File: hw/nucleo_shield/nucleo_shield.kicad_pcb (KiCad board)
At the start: 2 copper layers, 100 x 70 mm, 36 parts, among them CN101 Nucleo-F411RE-CN10, CN71 Nucleo-F411RE-CN7, P1 CONN_01X10, P2 CONN_01X10, P3 CONN_01X10, P4 CONN_01X02, P5 CONN_01X06, U1 74HC595, U2 74HC595, U3 LTV-847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

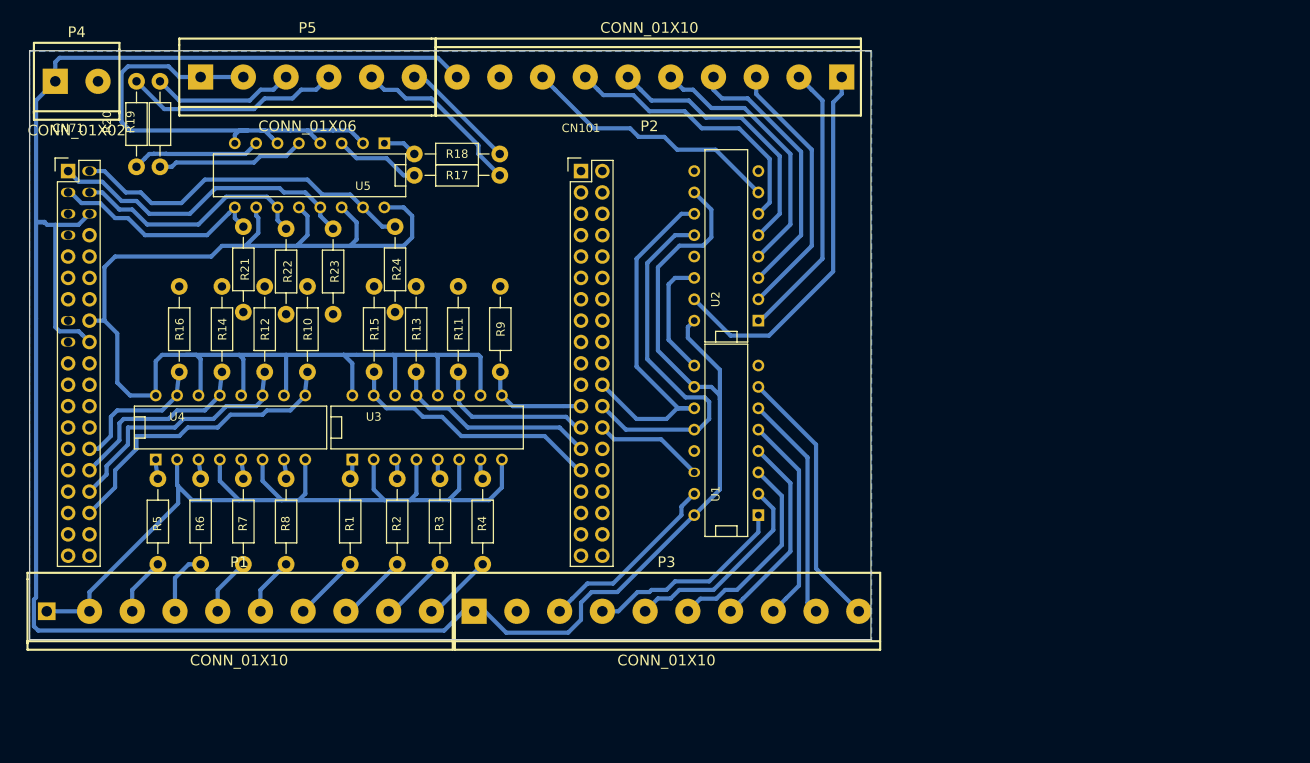
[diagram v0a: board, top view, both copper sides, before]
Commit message: HW: modify nucleo with hierarchical sheets
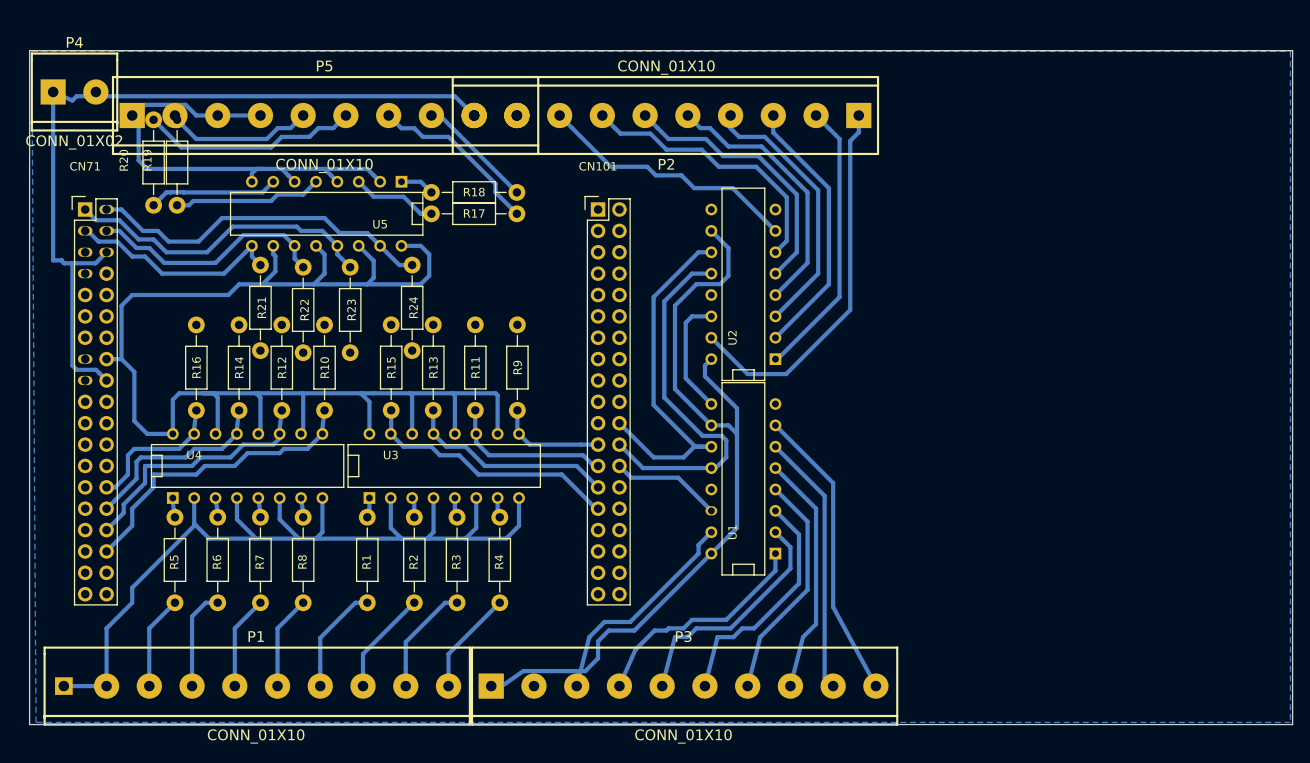
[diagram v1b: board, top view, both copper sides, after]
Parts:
- P5: value CONN_01X06 -> CONN_01X10; footprint w_conn_screw:mors_6p -> w_conn_screw:mors_10p
- moved P3 9.12 mm to (173.2, 144.0)
- moved P1 9.12 mm to (122.4, 144.0)
- moved R3 5.00 mm to (146.3, 129.0)
- moved R7 5.00 mm to (122.9, 129.0)
- moved R5 5.00 mm to (112.8, 129.0)
- moved R6 5.00 mm to (117.9, 129.0)
- moved R8 5.00 mm to (128.0, 129.0)
- moved R1 5.00 mm to (135.6, 129.0)
- moved R2 5.00 mm to (141.2, 129.0)
- moved R4 5.00 mm to (151.4, 129.0)
- moved CN101 5.00 mm to (163.1, 87.4)
- moved CN71 5.00 mm to (102.1, 87.4)
- moved P2 5.00 mm to (171.2, 76.2)
- moved P5 5.00 mm to (130.6, 76.2)
- moved R10 5.00 mm to (130.6, 106.2)
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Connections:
- P5 pad 3: inh11 -> inh16
- P5 pad 4: inh12 -> inh15
- P5 pad 5: inh10 -> inh14
- P5 pad 6: inh9 -> inh13
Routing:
- net +5V: track 291.6 -> 192.3 mm
- net inh10: track 20.7 -> 4.61 mm
- net inh16: track 0.00 -> 14.2 mm
- net inh9: track 13.9 -> 0.00 mm
- net inh12: track 25.8 -> 37.6 mm
- net inh14: track 0.00 -> 5.48 mm
- net inh3: track 8.92 -> 14.3 mm
- net inh1: track 9.05 -> 14.2 mm
- net inh2: track 9.19 -> 13.7 mm
- net inh4: track 8.92 -> 13.4 mm
- net inh5: track 7.57 -> 11.9 mm
- net out7: track 27.0 -> 31.3 mm
- net inh8: track 7.79 -> 12.1 mm
- net inh7: track 6.85 -> 11.2 mm
- net inh6: track 8.40 -> 12.7 mm
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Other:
- board size 100 x 70 mm -> 150.1 x 80.1 mm

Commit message: Update schematic to add sct and io expander
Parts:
- added P6: ETH_CONN, Pin_Headers:Pin_Header_Straight_2x04, F.Cu at (235.2, 114.0)
- added P7: SD_CONN, Pin_Headers:Pin_Header_Straight_1x05, F.Cu at (227.1, 114.0)
- added P8: LCD_CONN, Pin_Headers:Pin_Header_Straight_1x09, F.Cu at (218.8, 114.0)
- added R25: R, Resistors_ThroughHole:Resistor_Horizontal_RM10mm, F.Cu at (229.0, 78.8)
- added R26: R, Resistors_ThroughHole:Resistor_Horizontal_RM10mm, F.Cu at (242.5, 78.8)
- added R27: R, Resistors_ThroughHole:Resistor_Horizontal_RM10mm, F.Cu at (229.0, 88.5)
- added R28: R, Resistors_ThroughHole:Resistor_Horizontal_RM10mm, F.Cu at (242.5, 88.5)
- added R29: R, Resistors_ThroughHole:Resistor_Horizontal_RM10mm, F.Cu at (229.0, 98.3)
- added R30: R, Resistors_ThroughHole:Resistor_Horizontal_RM10mm, F.Cu at (256.0, 78.8)
- added R31: R, Resistors_ThroughHole:Resistor_Horizontal_RM10mm, F.Cu at (242.5, 98.3)
- added R32: R, Resistors_ThroughHole:Resistor_Horizontal_RM10mm, F.Cu at (256.0, 88.5)
- added R33: R_LCD_LED, Resistors_ThroughHole:Resistor_Horizontal_RM10mm, F.Cu at (241.6, 112.4)
- added R34: R, Resistors_ThroughHole:Resistor_Horizontal_RM10mm, F.Cu at (224.8, 131.1)
- added U6: LTV-847, Housings_DIP:DIP-16_W7.62mm, F.Cu at (218.2, 80.5)
- added U7: PCF8574A, Housings_DIP:DIP-16_W7.62mm, F.Cu at (276.2, 80.5)
- added U8: PCF8574A, Housings_DIP:DIP-16_W7.62mm, F.Cu at (289.6, 80.5)
- P4: value CONN_01X02 -> POWER_CON
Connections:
- CN101 pad 1: Net-(CN101-Pad1) -> IO_INT
- CN101 pad 11: Net-(CN101-Pad11) -> SPI1_SCK
- CN101 pad 13: Net-(CN101-Pad13) -> SPI1_MISO
- CN101 pad 15: Net-(CN101-Pad15) -> SPI1_MOSI
- CN101 pad 17: Net-(CN101-Pad17) -> SD_CS
- CN101 pad 19: Net-(CN101-Pad19) -> LCD_CS
- CN101 pad 21: Net-(CN101-Pad21) -> LCD_RST
- CN101 pad 23: in4 -> LCD_DC
- CN101 pad 25: in3 -> Net-(CN101-Pad25)
- CN101 pad 27: in2 -> Net-(CN101-Pad27)
- CN101 pad 29: in1 -> Net-(CN101-Pad29)
- CN101 pad 3: Net-(CN101-Pad3) -> I2C1_SCL
- CN101 pad 5: Net-(CN101-Pad5) -> I2C1_SDA
- CN71 pad 1: in10 -> SPI3_SCK
- CN71 pad 2: in9 -> SPI3_MISO
- CN71 pad 28: in5 -> Net-(CN71-Pad28)
- CN71 pad 3: in12 -> SPI3_MOSI
- CN71 pad 30: in6 -> Net-(CN71-Pad30)
- CN71 pad 32: in7 -> Net-(CN71-Pad32)
- CN71 pad 34: in8 -> Net-(CN71-Pad34)
- CN71 pad 4: in11 -> Net-(CN71-Pad4)
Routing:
- net SPI3_MISO: track 0.00 -> 31.2 mm
- net in9: track 41.4 -> 10.2 mm
- net in10: track 37.5 -> 8.23 mm
- net SPI3_SCK: track 0.00 -> 29.2 mm
- net in8: track 36.5 -> 8.30 mm
- net Net-(CN71-Pad34): track 0.00 -> 28.2 mm
- net Net-(CN101-Pad29): track 0.00 -> 22.9 mm
- net in1: track 30.9 -> 8.01 mm
- net in7: track 30.5 -> 15.4 mm
- net Net-(CN71-Pad32): track 0.00 -> 15.1 mm
- net in11: track 29.0 -> 14.3 mm
- net Net-(CN71-Pad4): track 0.00 -> 14.8 mm
- net in6: track 23.6 -> 9.04 mm
- net Net-(CN71-Pad30): track 0.00 -> 14.6 mm
- net Net-(CN101-Pad25): track 0.00 -> 13.5 mm
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
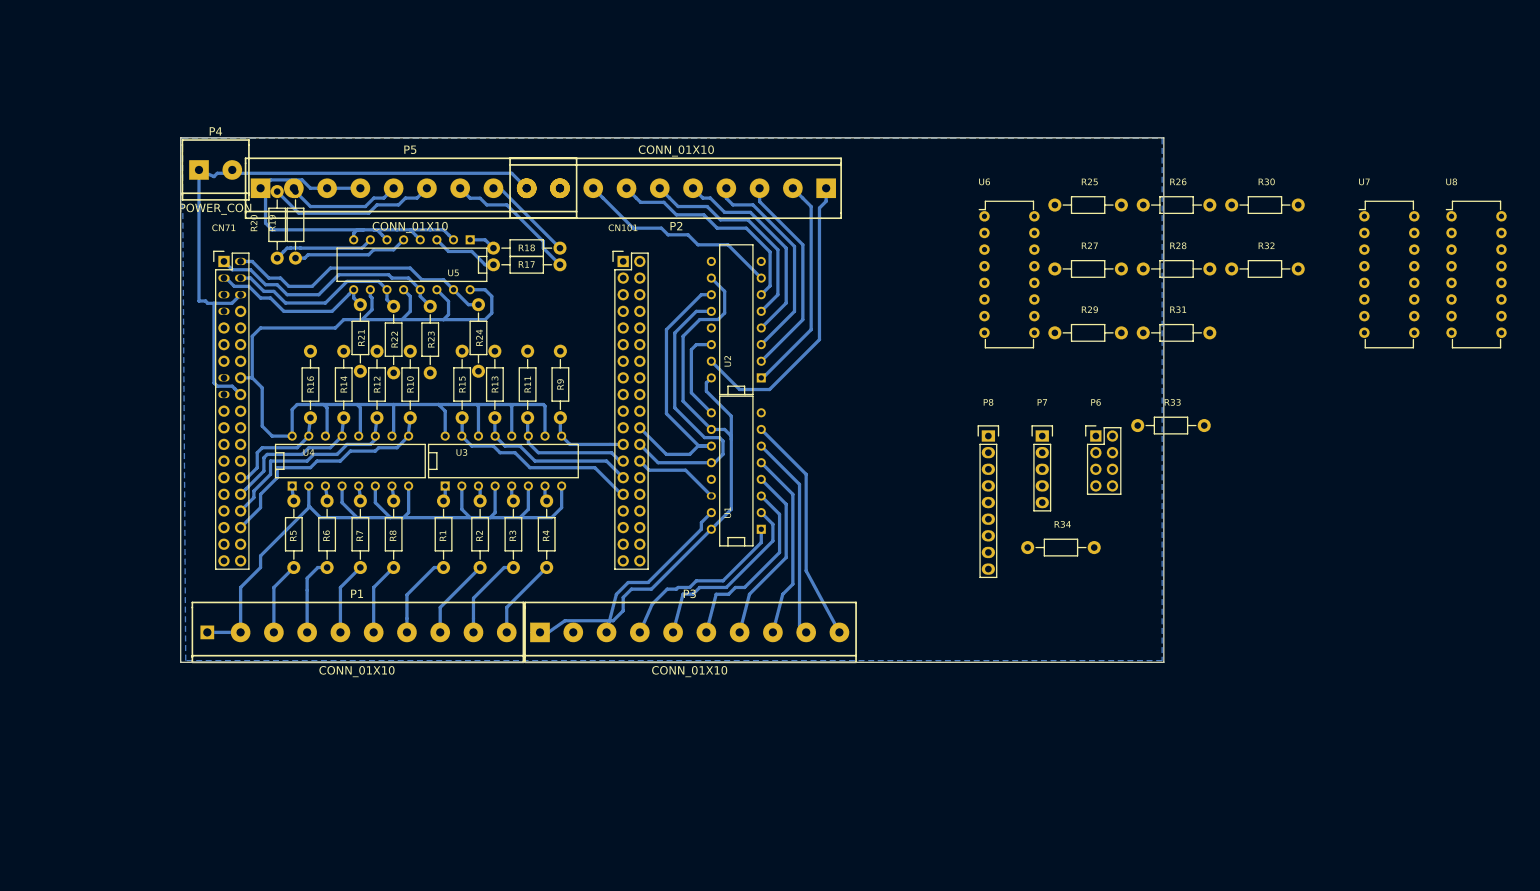
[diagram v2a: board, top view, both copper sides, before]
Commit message: Hw: add intermediate header between output and ULN2803
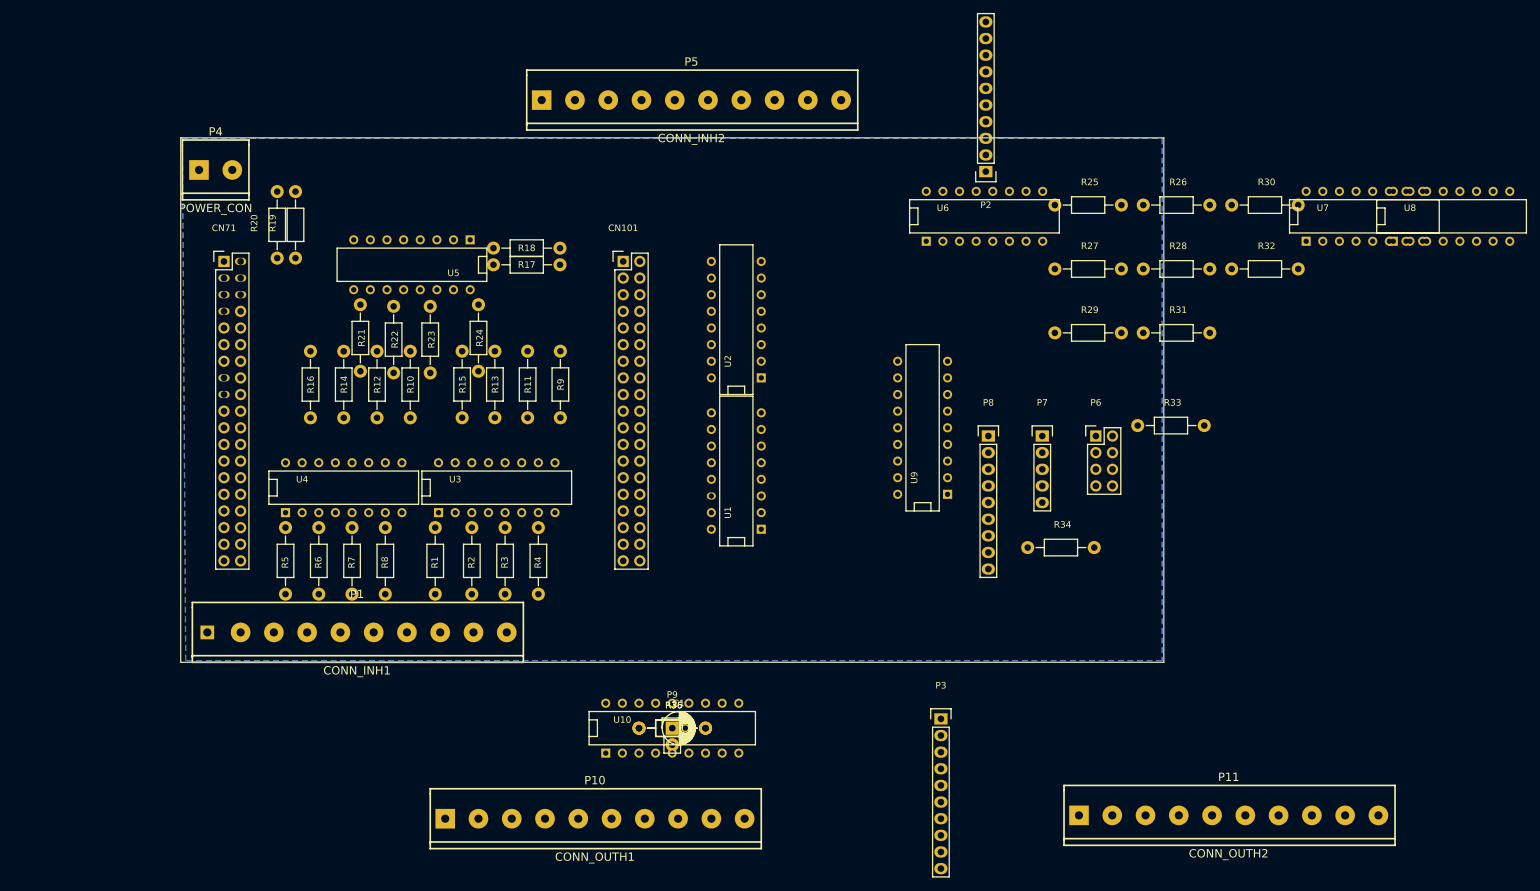
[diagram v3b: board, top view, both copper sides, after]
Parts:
- added C1: CP, Capacitors_ThroughHole:C_Radial_D5_L11_P2, F.Cu at (170.6, 158.6)
- added P10: CONN_OUTH1, w_conn_screw:mors_10p, F.Cu at (158.8, 172.5)
- added P11: CONN_OUTH2, w_conn_screw:mors_10p, F.Cu at (255.5, 172.0)
- added P9: CONN_SCT, Pin_Headers:Pin_Header_Straight_1x02, F.Cu at (170.6, 158.6)
- added R35, R36: R, Resistors_ThroughHole:Resistor_Horizontal_RM10mm, F.Cu at (170.6, 158.6)
- added U10: ULN2803, Housings_DIP:DIP-18__300, F.Cu at (170.6, 158.6)
- added U9: ULN2803, Housings_DIP:DIP-18__300, F.Cu at (208.8, 112.8)
- P1: value CONN_01X10 -> CONN_INH1
- P2: value CONN_01X10 -> CONN_OUT2; footprint w_conn_screw:mors_10p -> Pin_Headers:Pin_Header_Straight_1x10
- P3: value CONN_01X10 -> CONN_OUT1; footprint w_conn_screw:mors_10p -> Pin_Headers:Pin_Header_Straight_1x10
- P5: value CONN_01X10 -> CONN_INH2
- U6, U7, U8: footprint Housings_DIP:DIP-16_W7.62mm -> Housings_DIP:DIP-16__300
- moved P2 47.3 mm to (218.4, 73.7)
- moved P5 45.0 mm to (173.5, 62.7)
- moved P3 40.6 mm to (211.6, 157.2)
- moved R3 4.26 mm to (145.0, 133.1)
- moved R7 4.26 mm to (121.7, 133.1)
- moved R5 4.26 mm to (111.5, 133.1)
- moved R6 4.26 mm to (116.6, 133.1)
- moved R8 4.26 mm to (126.7, 133.1)
- moved R1 4.26 mm to (134.4, 133.1)
- moved R2 4.26 mm to (140.0, 133.1)
- moved R4 4.26 mm to (150.1, 133.1)
- moved U4 4.19 mm to (120.4, 121.9)
- moved U3 4.19 mm to (143.8, 121.9)
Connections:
- CN101 pad 23: LCD_DC -> Net-(CN101-Pad23)
- CN101 pad 25: Net-(CN101-Pad25) -> LCD_DC
- CN71 pad 28: Net-(CN71-Pad28) -> SCT_IN
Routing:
- net +5V: track 189.1 -> 0.00 mm
- net GND_24V: track 173.2 -> 0.00 mm
- net +3V3: track 162.2 -> 0.00 mm
- net out9: track 45.0 -> 0.00 mm
- net SRLatch: track 44.3 -> 0.00 mm
- net SRCLK: track 43.9 -> 0.00 mm
- net inh12: track 37.6 -> 0.00 mm
- net out8: track 36.2 -> 0.00 mm
- net out10: track 33.4 -> 0.00 mm
- net out15: track 33.0 -> 0.00 mm
- net out14: track 32.4 -> 0.00 mm
- net out12: track 32.1 -> 0.00 mm
- net out13: track 31.8 -> 0.00 mm
- net out11: track 31.8 -> 0.00 mm
- net out16: track 31.3 -> 0.00 mm
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
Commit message: HW: fix a lot of connection and start positionning
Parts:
- removed R10, R11, R12, R13, R14, R15, R16, R21, R22, R23, R24, R29, R30, R31, R32, R34, R9: R, Resistors_ThroughHole:Resistor_Horizontal_RM10mm
- moved U8 161.1 mm to (130.9, 108.8)
- moved P6 138.7 mm to (99.1, 87.6), turned to 90 degrees
- moved U7 125.7 mm to (153.8, 108.8)
- moved P11 104.9 mm to (220.3, 73.2), turned to 180 degrees
- moved R28 98.5 mm to (144.0, 86.9), turned to 45 degrees
- moved P9 89.0 mm to (97.7, 107.4)
- moved R26 88.7 mm to (154.1, 86.9), turned to 45 degrees
- moved R36 83.9 mm to (103.1, 108.6), turned to 90 degrees
- moved C1 83.5 mm to (98.1, 117.2)
- moved R35 81.4 mm to (103.0, 113.3), turned to 180 degrees
- moved R27 80.0 mm to (149.0, 86.9), turned to 45 degrees
- moved R25 70.3 mm to (159.2, 86.9), turned to 45 degrees
- moved P4 70.0 mm to (100.6, 143.4)
- moved U10 69.1 mm to (229.6, 122.6), turned to 270 degrees
- moved P10 67.4 mm to (219.9, 144.0)
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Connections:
- CN101 pad 10: Net-(CN101-Pad10) -> (no net)
- CN101 pad 12: Net-(CN101-Pad12) -> (no net)
- CN101 pad 14: Net-(CN101-Pad14) -> (no net)
- CN101 pad 16: Net-(CN101-Pad16) -> (no net)
- CN101 pad 18: Net-(CN101-Pad18) -> (no net)
- CN101 pad 2: Net-(CN101-Pad2) -> (no net)
- CN101 pad 23: Net-(CN101-Pad23) -> (no net)
- CN101 pad 27: Net-(CN101-Pad27) -> (no net)
- CN101 pad 28: Net-(CN101-Pad28) -> (no net)
- CN101 pad 29: Net-(CN101-Pad29) -> (no net)
- CN101 pad 30: Net-(CN101-Pad30) -> (no net)
- CN101 pad 31: Net-(CN101-Pad31) -> (no net)
- CN101 pad 32: Net-(CN101-Pad32) -> (no net)
- CN101 pad 33: Net-(CN101-Pad33) -> (no net)
- CN101 pad 34: Net-(CN101-Pad34) -> (no net)
- CN101 pad 35: Net-(CN101-Pad35) -> (no net)
- CN101 pad 36: Net-(CN101-Pad36) -> (no net)
- CN101 pad 37: Net-(CN101-Pad37) -> (no net)
- CN101 pad 38: Net-(CN101-Pad38) -> (no net)
- CN101 pad 4: Net-(CN101-Pad4) -> (no net)
- CN101 pad 6: Net-(CN101-Pad6) -> (no net)
- CN101 pad 7: Net-(CN101-Pad7) -> (no net)
- CN101 pad 8: Net-(CN101-Pad8) -> (no net)
- CN71 pad 10: Net-(CN71-Pad10) -> (no net)
- CN71 pad 11: Net-(CN71-Pad11) -> (no net)
- CN71 pad 12: Net-(CN71-Pad12) -> (no net)
- CN71 pad 13: Net-(CN71-Pad13) -> (no net)
- CN71 pad 14: Net-(CN71-Pad14) -> (no net)
- CN71 pad 15: Net-(CN71-Pad15) -> (no net)
- CN71 pad 17: Net-(CN71-Pad17) -> (no net)
- CN71 pad 21: Net-(CN71-Pad21) -> (no net)
- CN71 pad 23: Net-(CN71-Pad23) -> (no net)
- CN71 pad 24: Net-(CN71-Pad24) -> (no net)
- CN71 pad 25: Net-(CN71-Pad25) -> (no net)
- CN71 pad 26: Net-(CN71-Pad26) -> (no net)
- CN71 pad 27: Net-(CN71-Pad27) -> (no net)
- CN71 pad 29: Net-(CN71-Pad29) -> (no net)
- CN71 pad 30: Net-(CN71-Pad30) -> (no net)
- CN71 pad 31: Net-(CN71-Pad31) -> (no net)
- CN71 pad 32: Net-(CN71-Pad32) -> (no net)
- CN71 pad 33: Net-(CN71-Pad33) -> (no net)
- CN71 pad 34: Net-(CN71-Pad34) -> (no net)
- CN71 pad 35: Net-(CN71-Pad35) -> (no net)
- CN71 pad 36: Net-(CN71-Pad36) -> (no net)
- CN71 pad 37: Net-(CN71-Pad37) -> (no net)
- CN71 pad 38: Net-(CN71-Pad38) -> (no net)
- CN71 pad 4: Net-(CN71-Pad4) -> (no net)
- CN71 pad 7: Net-(CN71-Pad7) -> (no net)
- CN71 pad 9: Net-(CN71-Pad9) -> (no net)
- P6 pad 3: ETH_CS -> (no net)
- P6 pad 4: ETH_RST -> (no net)
- P7 pad 5: Net-(P7-Pad5) -> (no net)
- R17 pad 2: inh9 -> inh11
- R18 pad 2: inh10 -> inh12
- R19 pad 2: inh11 -> inh10
- R20 pad 2: inh12 -> inh9
- R25 pad 2: inh13 -> inh16
- R26 pad 2: inh14 -> inh15
- R27 pad 2: inh15 -> inh14
- R28 pad 2: inh16 -> inh13
- U10 pad 1: out1 -> out8
- U10 pad 11: out8h -> out1h
- U10 pad 12: out7h -> out2h
- U10 pad 13: out6h -> out3h
- U10 pad 14: out5h -> out4h
- U10 pad 15: out4h -> out5h
- U10 pad 16: out3h -> out6h
- U10 pad 17: out2h -> out7h
- U10 pad 18: out1h -> out8h
- U10 pad 2: out2 -> out7
- U10 pad 3: out3 -> out6
- U10 pad 4: out4 -> out5
- U10 pad 5: out5 -> out4
- U10 pad 6: out6 -> out3
- U10 pad 7: out7 -> out2
- U10 pad 8: out8 -> out1
- U2 pad 9: Net-(U2-Pad9) -> (no net)
- U7 pad 4: in9 -> in1
- U7 pad 5: in10 -> in2
- U7 pad 6: in11 -> in3
- U7 pad 7: in12 -> in4
- U8 pad 10: in6 -> in10
- U8 pad 11: in7 -> in11
- U8 pad 12: in8 -> in12
- U8 pad 4: in1 -> in5
- U8 pad 5: in2 -> in6
- U8 pad 6: in3 -> in7
- U8 pad 7: in4 -> in8
- U8 pad 9: in5 -> in9
- U9 pad 1: out9 -> out16
- U9 pad 11: out16h -> out9h
- U9 pad 12: out15h -> out10h
- U9 pad 13: out14h -> out11h
- U9 pad 14: out13h -> out12h
- U9 pad 15: out12h -> out13h
- U9 pad 16: out11h -> out14h
- U9 pad 17: out10h -> out15h
- U9 pad 18: out9h -> out16h
- U9 pad 2: out10 -> out15
- U9 pad 3: out11 -> out14
- U9 pad 4: out12 -> out13
- U9 pad 5: out13 -> out12
- U9 pad 6: out14 -> out11
- U9 pad 7: out15 -> out10
- U9 pad 8: out16 -> out9
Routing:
- net I2C1_SCL: track 0.00 -> 64.7 mm
- net I2C1_SDA: track 0.00 -> 64.2 mm
- net IO_INT: track 0.00 -> 37.1 mm
